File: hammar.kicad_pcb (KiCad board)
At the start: 2 copper layers, 97.5 x 55 mm, 118 parts, among them J1 8x screw terminal, 5,08mm spa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, J10 1x2, J11 1x4, J12 1x3, J13 1x8, J2 Micro_SD_Holder, J3 USB_C_Receptacle_USB2.0, J4 1x4, J5 1x4, J6 1x4, J7 1x4, J8 1x4, J9 1x2, Q1 S9014 or equivalent, Q2 S9014 or equivalent, Q3 TI CSD17310Q5A or equivalent, Q4 PMV40UN2R or equivalent, Q5 PMV40UN2R or equivalent, SW1 SW_MEC_5G, U1 A4988, U2 A4988, U3 A4988, U4 A4988, U5 DPAK 3,3v linear regulator + 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, U6 ESP32-WROOM-32E, U7 CH340G, Y1 Resonator_12mhz

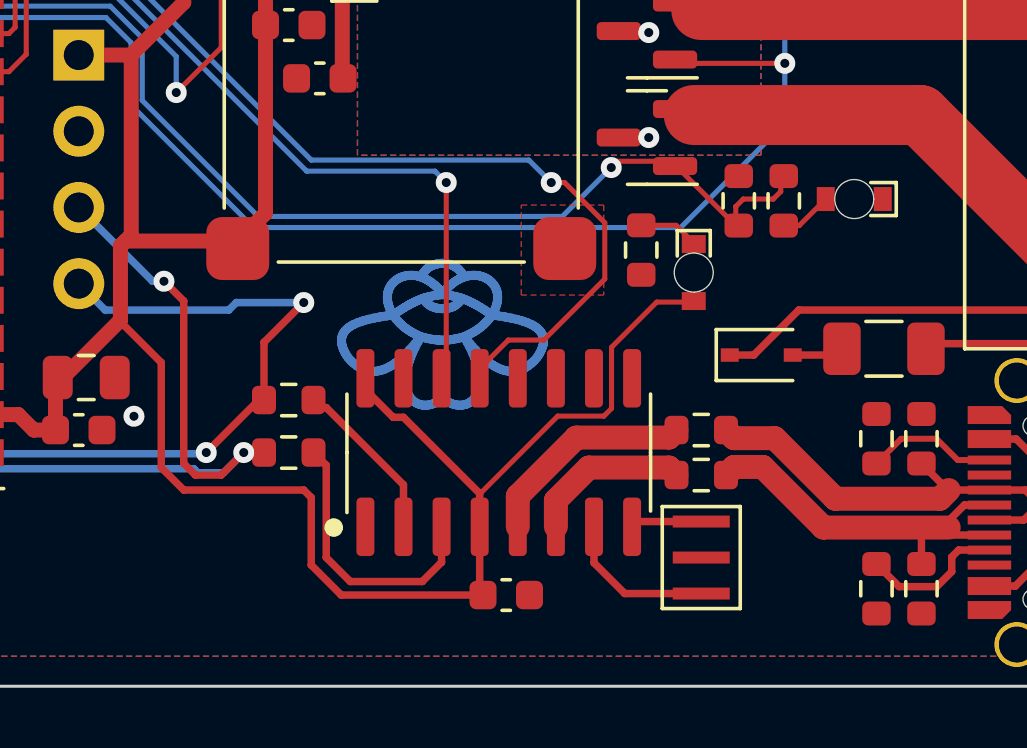
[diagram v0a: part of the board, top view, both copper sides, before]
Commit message: replaced oscillator with crystal
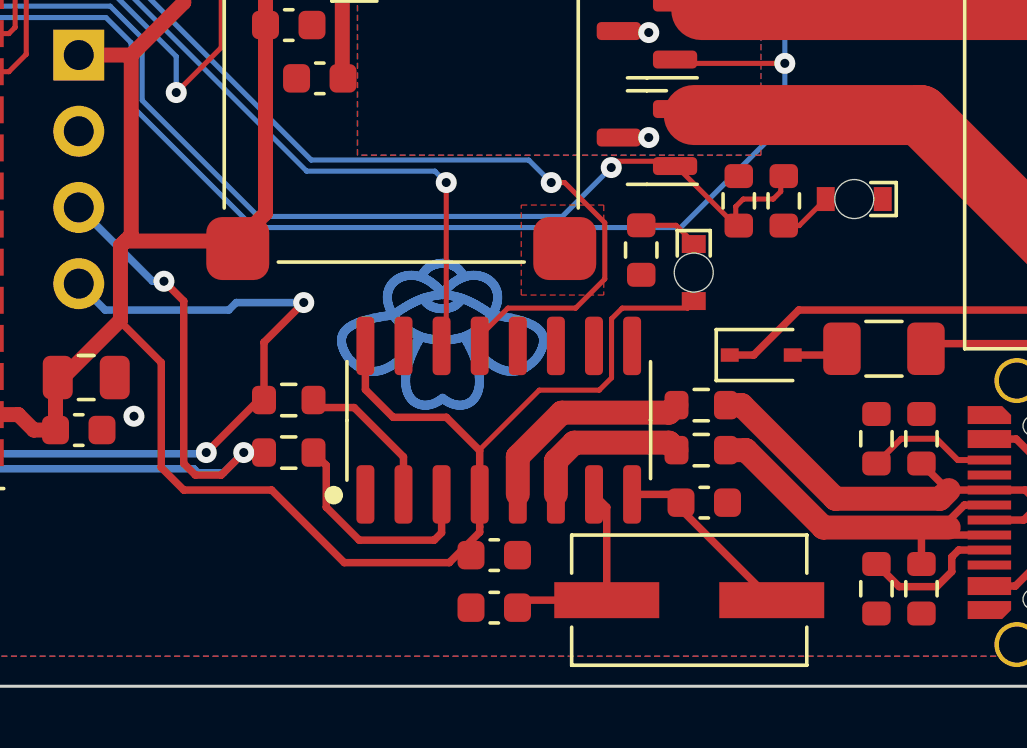
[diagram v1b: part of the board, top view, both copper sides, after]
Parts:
- added C29: 22pF, Capacitor_SMD:C_0603_1608Metric, F.Cu at (165.1, 118.1)
- added C30: 22pF, Capacitor_SMD:C_0603_1608Metric, F.Cu at (172.1, 114.6)
- Y1: value Resonator_12mhz -> Crystal_12mhz; footprint DIY:resonator_3,2x1,3 -> Crystal:Crystal_SMD_ECS_CSM3X-2Pin_7.6x4.1mm
- moved Y1 1.48 mm to (171.6, 117.9), turned to 0 degrees
- moved C28 1.39 mm to (165.1, 116.4)
- moved U7 1.08 mm to (165.2, 111.9)
- moved R39 0.83 mm to (172.0, 111.4)
- moved R42 0.83 mm to (172.0, 112.9)
- renumbered X to J14, Z to J15, Y to J16
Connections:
- U7 pad 8: Net-(U7-Pad8) -> Net-(C30-Pad1)
- Y1 pad 2: GND -> Net-(C30-Pad1)
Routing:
- net Net-(C30-Pad1): track 0.00 -> 6.25 mm
- net Net-(U7-Pad8): track 2.38 -> 0.00 mm
- net Net-(R41-Pad1): track 9.30 -> 7.68 mm
- net Net-(C29-Pad1): track 5.20 -> 6.78 mm
- net RTS: track 47.6 -> 46.5 mm
- net +3.3V: track 375.8 -> 375.0 mm
- net Net-(R38-Pad2): track 5.47 -> 4.93 mm

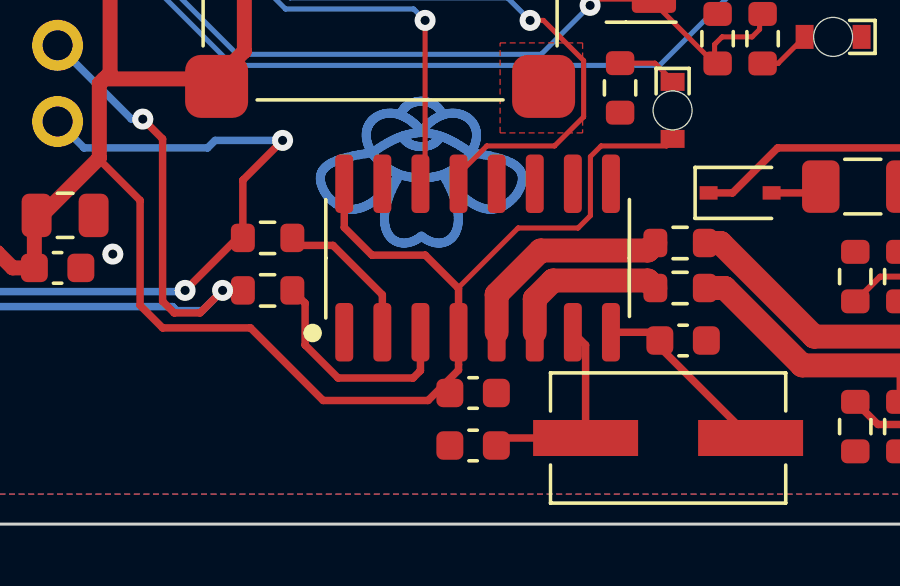
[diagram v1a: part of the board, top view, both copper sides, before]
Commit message: removed possibly problematic trace
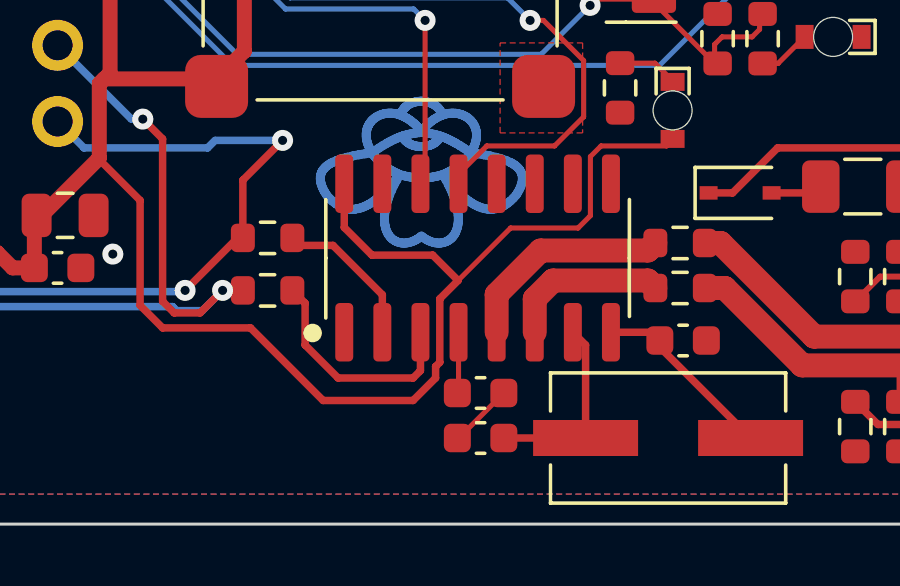
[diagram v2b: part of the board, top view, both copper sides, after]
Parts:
- moved C29 0.35 mm to (165.3, 117.9)
- moved C28 0.25 mm to (165.3, 116.4)
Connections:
- C28 pad 2: +3.3V -> Net-(C28-Pad2)
- U7 pad 4: +3.3V -> Net-(C28-Pad2)
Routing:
- net +3.3V: track 375.0 -> 372.2 mm
- net GND: track 48.9 -> 51.1 mm
- net Net-(C28-Pad2): track 0.00 -> 2.15 mm
